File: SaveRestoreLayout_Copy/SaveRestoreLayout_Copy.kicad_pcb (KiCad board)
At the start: 2 copper layers, 3 parts

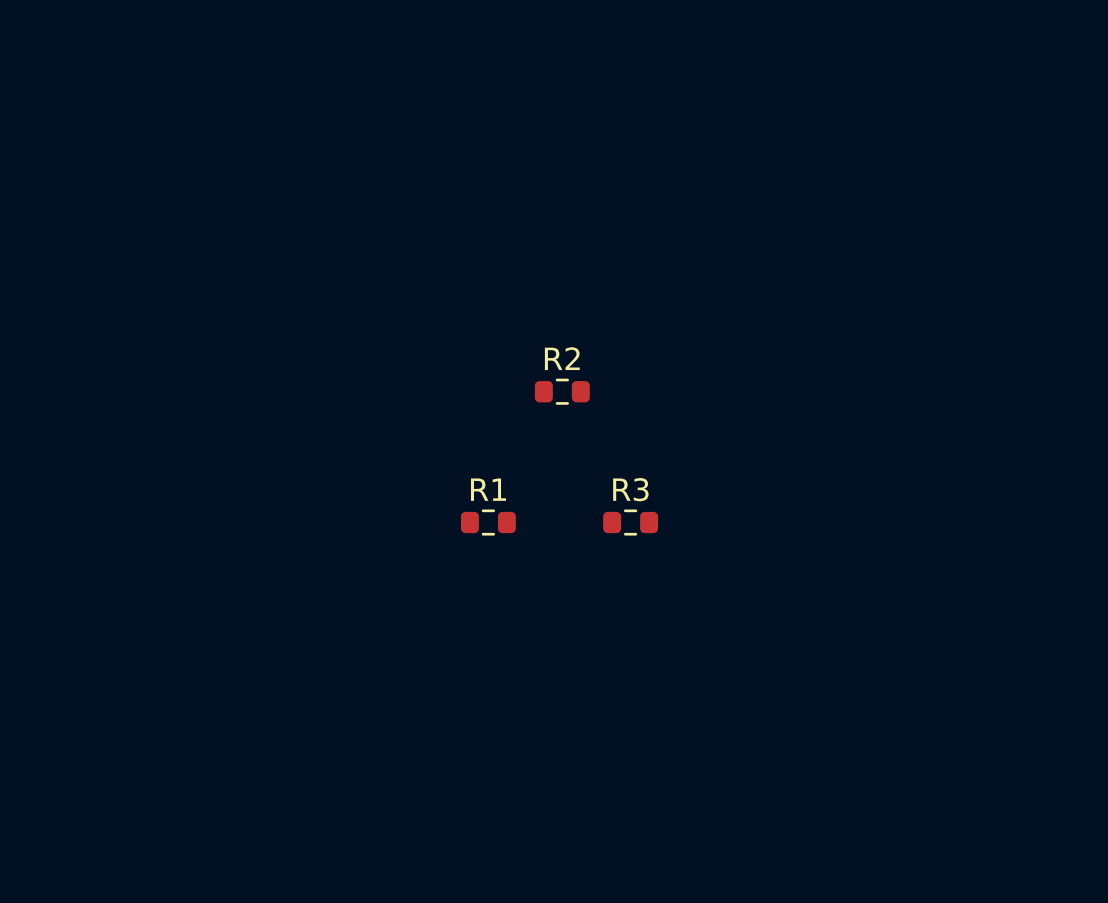
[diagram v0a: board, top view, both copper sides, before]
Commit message: restore the layour from original
bug: the bottom layout is not restored and no via is placed
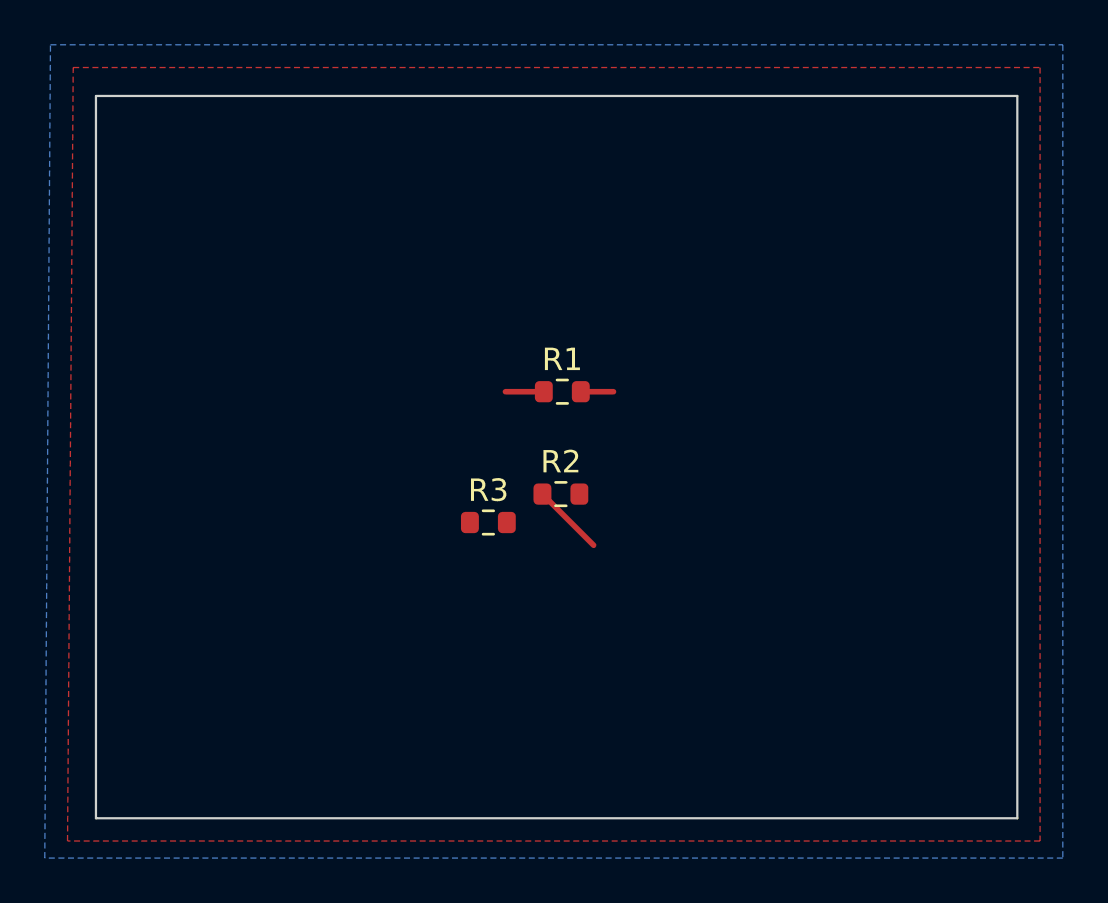
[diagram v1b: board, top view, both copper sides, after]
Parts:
- moved R2 3.36 mm to (121.5, 76.7)
- renumbered R2 to R1, R3 to R2, R1 to R3
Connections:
- R3 pad 1: +3.3V -> +3V3
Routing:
- net Net-(R1-Pad2): track 0.00 -> 4.69 mm
- net +3V3: track 0.00 -> 1.72 mm
- added copper zone on B.Cu, net +3V3
- added copper zone on F.Cu, net GND
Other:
- board outline added: 41.1 x 32.3 mm
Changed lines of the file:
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@@
   )
   (net 0 "")
-  (net 1 "+3.3V")
+  (net 1 "Net-(R1-Pad2)")
   (net 2 "GND")
   (net 3 "+3V3")
-  (net 4 "Net-(R2-Pad2)")
   (footprint "Resistor_SMD:R_0603_1608Metric" (layer "F.Cu")
     (at 118.301 77.978)
@@
     (property "ki_keywords" "R res resistor")
     (attr smd)
-    (fp_text reference "R1" (at 0 -1.43) (layer "F.SilkS")
+    (fp_text reference "R3" (at 0 -1.43) (layer "F.SilkS")
         (effects (font (size 1 1) (thickness 0.15)))
     )
@@
       (stroke (width 0.1) (type solid)) (layer "F.Fab"))
     (pad "1" smd roundrect (at -0.825 0) (size 0.8 0.95) (layers "F.Cu" "F.Paste" "F.Mask") (roundrect_rratio 0.25)
-      (net 1 "+3.3V") (pintype "passive"))
+      (net 3 "+3V3") (pintype "passive"))
     (pad "2" smd roundrect (at 0.825 0) (size 0.8 0.95) (layers "F.Cu" "F.Paste" "F.Mask") (roundrect_rratio 0.25)
       (net 2 "GND") (pintype "passive"))
@@
   (footprint "Resistor_SMD:R_0603_1608Metric" (layer "F.Cu")
     (at 121.603 72.136)
+    (descr "Resistor SMD 0603 (1608 Metric), square (rectangular) end terminal, IPC_7351 nominal, (Body size source: IPC-SM-782 page 72, https://www.pcb-3d.com/wordpress/wp-content/uploads/ipc-sm-782a_amendment_1_and_2.pdf), generated with kicad-footprint-generator")
+    (tags "resistor")
+    (property "Sheetfile" "U_half.kicad_sch")
+    (property "Sheetname" "half voltage")
+    (property "ki_description" "Resistor")
+    (property "ki_keywords" "R res resistor")
+    (attr smd)
+    (fp_text reference "R1" (at 0 -1.43) (layer "F.SilkS")
+        (effects (font (size 1 1) (thickness 0.15)))
+    )
+    (fp_text value "10k" (at 0 1.43) (layer "F.Fab")
+        (effects (font (size 1 1) (thickness 0.15)))
+    )
+    (fp_text user "${REFERENCE}" (at 0 0) (layer "F.Fab")
+        (effects (font (size 0.4 0.4) (thickness 0.06)))
+    )
+    (fp_line (start -0.237258 -0.5225) (end 0.237258 -0.5225)
+      (stroke (width 0.12) (type solid)) (layer "F.SilkS"))
+    (fp_line (start -0.237258 0.5225) (end 0.237258 0.5225)
+      (stroke (width 0.12) (type solid)) (layer "F.SilkS"))
+    (fp_line (start -1.48 -0.73) (end 1.48 -0.73)
+      (stroke (width 0.05) (type solid)) (layer "F.CrtYd"))
+    (fp_line (start -1.48 0.73) (end -1.48 -0.73)
+      (stroke (width 0.05) (type solid)) (layer "F.CrtYd"))
+    (fp_line (start 1.48 -0.73) (end 1.48 0.73)
+      (stroke (width 0.05) (type solid)) (layer "F.CrtYd"))
+    (fp_line (start 1.48 0.73) (end -1.48 0.73)
+      (stroke (width 0.05) (type solid)) (layer "F.CrtYd"))
+    (fp_line (start -0.8 -0.4125) (end 0.8 -0.4125)
+      (stroke (width 0.1) (type solid)) (layer "F.Fab"))
+    (fp_line (start -0.8 0.4125) (end -0.8 -0.4125)
+      (stroke (width 0.1) (type solid)) (layer "F.Fab"))
+    (fp_line (start 0.8 -0.4125) (end 0.8 0.4125)
+      (stroke (width 0.1) (type solid)) (layer "F.Fab"))
+    (fp_line (start 0.8 0.4125) (end -0.8 0.4125)
+      (stroke (width 0.1) (type solid)) (layer "F.Fab"))
+    (pad "1" smd roundrect (at -0.825 0) (size 0.8 0.95) (layers "F.Cu" "F.Paste" "F.Mask") (roundrect_rratio 0.25)
+      (net 3 "+3V3") (pintype "passive"))
+    (pad "2" smd roundrect (at 0.825 0) (size 0.8 0.95) (layers "F.Cu" "F.Paste" "F.Mask") (roundrect_rratio 0.25)
+      (net 1 "Net-(R1-Pad2)") (pintype "passive"))
+    (model "${KICAD6_3DMODEL_DIR}/Resistor_SMD.3dshapes/R_0603_1608Metric.wrl"
+      (offset (xyz 0 0 0))
+      (scale (xyz 1 1 1))
+      (rotate (xyz 0 0 0))
+    )
+  )
+  (footprint "Resistor_SMD:R_0603_1608Metric" (layer "F.Cu")
+    (at 121.54 76.708)
     (descr "Resistor SMD 0603 (1608 Metric), square (rectangular) end terminal, IPC_7351 nominal, (Body size source: IPC-SM-782 page 72, https://www.pcb-3d.com/wordpress/wp-content/uploads/ipc-sm-782a_amendment_1_and_2.pdf), generated with kicad-footprint-generator")
     (tags "resistor")
@@
       (stroke (width 0.1) (type solid)) (layer "F.Fab"))
     (pad "1" smd roundrect (at -0.825 0) (size 0.8 0.95) (layers "F.Cu" "F.Paste" "F.Mask") (roundrect_rratio 0.25)
-      (net 3 "+3V3") (pintype "passive"))
-    (pad "2" smd roundrect (at 0.825 0) (size 0.8 0.95) (layers "F.Cu" "F.Paste" "F.Mask") (roundrect_rratio 0.25)
-      (net 4 "Net-(R2-Pad2)") (pintype "passive"))
-    (model "${KICAD6_3DMODEL_DIR}/Resistor_SMD.3dshapes/R_0603_1608Metric.wrl"
-      (offset (xyz 0 0 0))
-      (scale (xyz 1 1 1))
-      (rotate (xyz 0 0 0))
-    )
-  )
-  (footprint "Resistor_SMD:R_0603_1608Metric" (layer "F.Cu")
-    (at 124.651 77.978)
-    (descr "Resistor SMD 0603 (1608 Metric), square (rectangular) end terminal, IPC_7351 nominal, (Body size source: IPC-SM-782 page 72, https://www.pcb-3d.com/wordpress/wp-content/uploads/ipc-sm-782a_amendment_1_and_2.pdf), generated with kicad-footprint-generator")
-    (tags "resistor")
-    (property "Sheetfile" "U_half.kicad_sch")
-    (property "Sheetname" "half voltage")
-    (property "ki_description" "Resistor")
-    (property "ki_keywords" "R res resistor")
-    (attr smd)
-    (fp_text reference "R3" (at 0 -1.43) (layer "F.SilkS")
-        (effects (font (size 1 1) (thickness 0.15)))
-    )
-    (fp_text value "10k" (at 0 1.43) (layer "F.Fab")
-        (effects (font (size 1 1) (thickness 0.15)))
-    )
-    (fp_text user "${REFERENCE}" (at 0 0) (layer "F.Fab")
-        (effects (font (size 0.4 0.4) (thickness 0.06)))
-    )
-    (fp_line (start -0.237258 -0.5225) (end 0.237258 -0.5225)
-      (stroke (width 0.12) (type solid)) (layer "F.SilkS"))
-    (fp_line (start -0.237258 0.5225) (end 0.237258 0.5225)
-      (stroke (width 0.12) (type solid)) (layer "F.SilkS"))
-    (fp_line (start -1.48 -0.73) (end 1.48 -0.73)
-      (stroke (width 0.05) (type solid)) (layer "F.CrtYd"))
-    (fp_line (start -1.48 0.73) (end -1.48 -0.73)
-      (stroke (width 0.05) (type solid)) (layer "F.CrtYd"))
-    (fp_line (start 1.48 -0.73) (end 1.48 0.73)
-      (stroke (width 0.05) (type solid)) (layer "F.CrtYd"))
-    (fp_line (start 1.48 0.73) (end -1.48 0.73)
-      (stroke (width 0.05) (type solid)) (layer "F.CrtYd"))
-    (fp_line (start -0.8 -0.4125) (end 0.8 -0.4125)
-      (stroke (width 0.1) (type solid)) (layer "F.Fab"))
-    (fp_line (start -0.8 0.4125) (end -0.8 -0.4125)
-      (stroke (width 0.1) (type solid)) (layer "F.Fab"))
-    (fp_line (start 0.8 -0.4125) (end 0.8 0.4125)
-      (stroke (width 0.1) (type solid)) (layer "F.Fab"))
-    (fp_line (start 0.8 0.4125) (end -0.8 0.4125)
-      (stroke (width 0.1) (type solid)) (layer "F.Fab"))
-    (pad "1" smd roundrect (at -0.825 0) (size 0.8 0.95) (layers "F.Cu" "F.Paste" "F.Mask") (roundrect_rratio 0.25)
-      (net 4 "Net-(R2-Pad2)") (pintype "passive"))
+      (net 1 "Net-(R1-Pad2)") (pintype "passive"))
     (pad "2" smd roundrect (at 0.825 0) (size 0.8 0.95) (layers "F.Cu" "F.Paste" "F.Mask") (roundrect_rratio 0.25)
       (net 2 "GND") (pintype "passive"))
@@
     )
   )
+  (gr_rect (start 100.775 58.928) (end 141.923 91.186)
+    (stroke (width 0.1) (type default)) (fill none) (layer "Edge.Cuts"))
+  (segment (start 122.428 72.136) (end 123.889 72.136) (width 0.25) (layer "F.Cu") (net 1))
+  (segment (start 123.001 78.994) (end 120.715 76.708) (width 0.25) (layer "F.Cu") (net 1))
+  (segment (start 120.778 72.136) (end 119.063 72.136) (width 0.25) (layer "F.Cu") (net 3))
+  (zone (net 2) (net_name "GND") (layer "F.Cu") (hatch edge 0.5)
+    (connect_pads (clearance 0.5))
+    (min_thickness 0.25) (filled_areas_thickness no)
+    (fill yes (thermal_gap 0.5) (thermal_bridge_width 0.5))
+    (polygon
+      (pts
+        (xy 99.759 57.658)
+        (xy 142.939 57.658)
+        (xy 142.939 92.202)
+        (xy 99.505 92.202)
+      )
+    )
+  )
+  (zone (net 3) (net_name "+3V3") (layer "B.Cu") (hatch edge 0.5)
+    (priority 1)
+    (connect_pads (clearance 0.5))
+    (min_thickness 0.25) (filled_areas_thickness no)
+    (fill yes (thermal_gap 0.5) (thermal_bridge_width 0.5))
+    (polygon
+      (pts
+        (xy 98.743 56.642)
+        (xy 143.955 56.642)
+        (xy 143.955 92.964)
+        (xy 98.489 92.964)
+      )
+    )
+  )
+  (group "restore_from_original" (id f50040ad-afee-4b1f-9d7b-52e4bfb7db15)
+    (members
+      49b020c7-a667-401d-b0ba-ba21048314f3
+      79d4c626-ec4a-4ea1-b453-83cc78c72588
+      7c858c88-f0eb-4fa7-a9ed-a6b5d431d461
+      9530f554-3f67-4216-821b-7e3072b2332a
+      f377d273-4039-418d-9be9-a94803178b0c
+      f4b0277b-deae-490c-be98-d2c05b71f823
+      f78241cd-8e21-4c94-8d72-1db545317dbb
+      f965b30d-682e-4a92-8de6-fb9692526f1b
+    )
+  )
